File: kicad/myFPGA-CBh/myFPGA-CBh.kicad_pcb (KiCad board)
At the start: 2 copper layers, 100 x 80 mm, 62 parts, among them J1 Conn_01x04, J10 Conn_01x04, J11 Conn_01x04, J12 Conn_01x04, J13 Conn_01x04, J14 Conn_01x04, J15 Conn_01x04, J2 Conn_01x04, J3 Conn_01x04, J4 Conn_01x04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

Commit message: start new feature CE
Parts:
- added D16: LED (green), LED_SMD:LED_0805_2012Metric, F.Cu at (177.0, 114.0)
- added J16: Conn_01x02, Connector_PinHeader_2.54mm:PinHeader_1x02_P2.54mm_Horizontal, F.Cu at (181.5, 125.0)
- added R16: 330R, Resistor_SMD:R_0603_1608Metric, F.Cu at (173.0, 115.0)
- added U10: BL1551B, Package_TO_SOT_SMD:SOT-363_SC-70-6, F.Cu at (177.0, 116.6)
- U7, U8, U9: value NC7SB3157P6X -> BL1551B
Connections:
- J7 pad 1: prio_0 -> bus_4
- J7 pad 2: prio_1 -> bus_5
- J8 pad 1: prio_1 -> bus_5
- J8 pad 2: prio_0 -> bus_4
- U2 pad 7: unconnected-(U2-QH-Pad7) -> xp_ce
- U3 pad 1: prio_0 -> unconnected-(U3-I3-Pad1)
- U3 pad 2: prio_1 -> unconnected-(U3-I2-Pad2)
- U4 pad 1: prio_0 -> bus_4
- U4 pad 2: prio_1 -> bus_5
- U5 pad 1: prio_0 -> bus_4
- U5 pad 2: prio_1 -> bus_5
- U6 pad 1: prio_0 -> bus_4
- U6 pad 2: prio_1 -> bus_5
- U7 pad 4: prio_0 -> bus_4
- U8 pad 4: prio_1 -> bus_5
- U9 pad 4: prio_0 -> bus_4
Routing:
- net (no net): track 0.00 -> 415.0 mm, vias 0 -> 13
- net prio_0: track 214.8 -> 0.00 mm, vias 7 -> 0
- net prio_1: track 200.3 -> 0.00 mm, vias 6 -> 0
- net xp_ce: track 0.00 -> 73.4 mm, vias 0 -> 2
- net GND: track 514.0 -> 522.2 mm, vias 16 -> 17
- net ce: track 0.00 -> 8.19 mm
- net +3.3VP: track 145.2 -> 148.7 mm, vias 13 -> 14
- net Net-(D16-A): track 0.00 -> 3.13 mm
- net aresetn: track 69.3 -> 72.2 mm

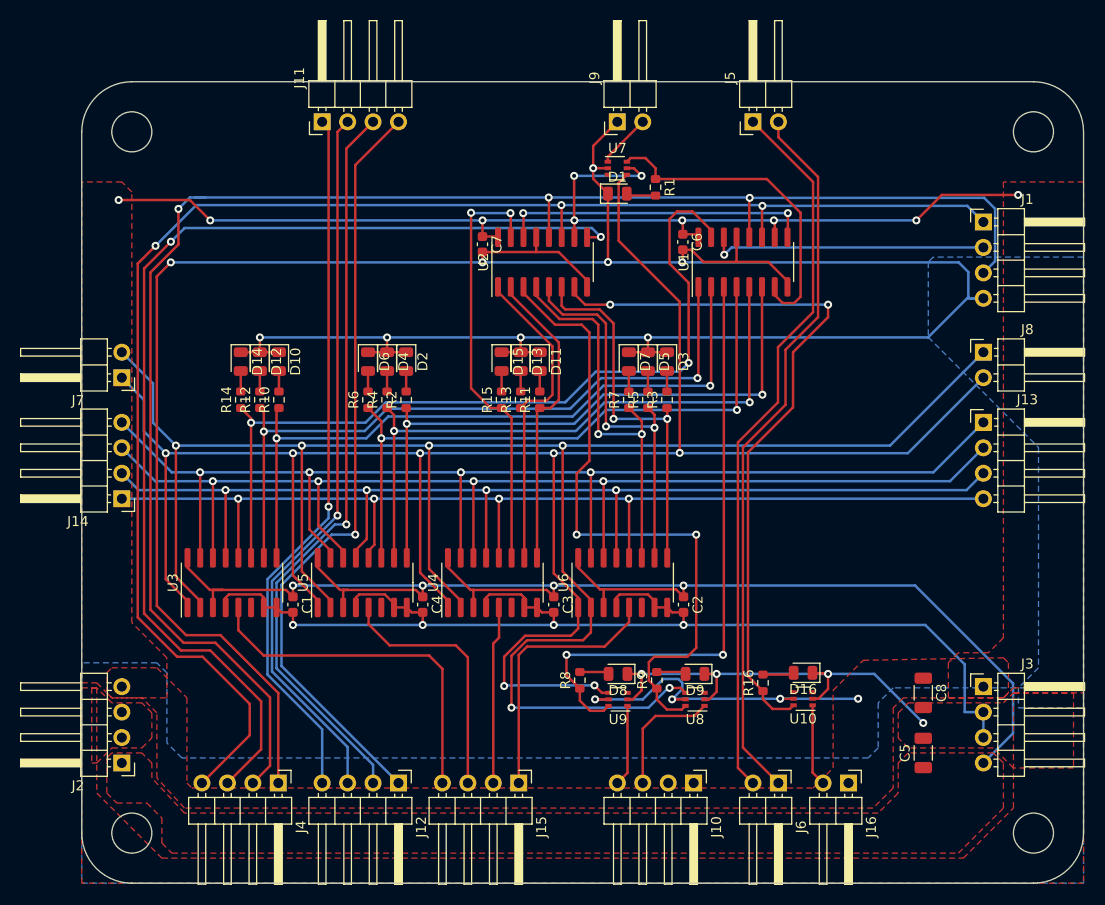
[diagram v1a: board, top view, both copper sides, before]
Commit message: found more bugs
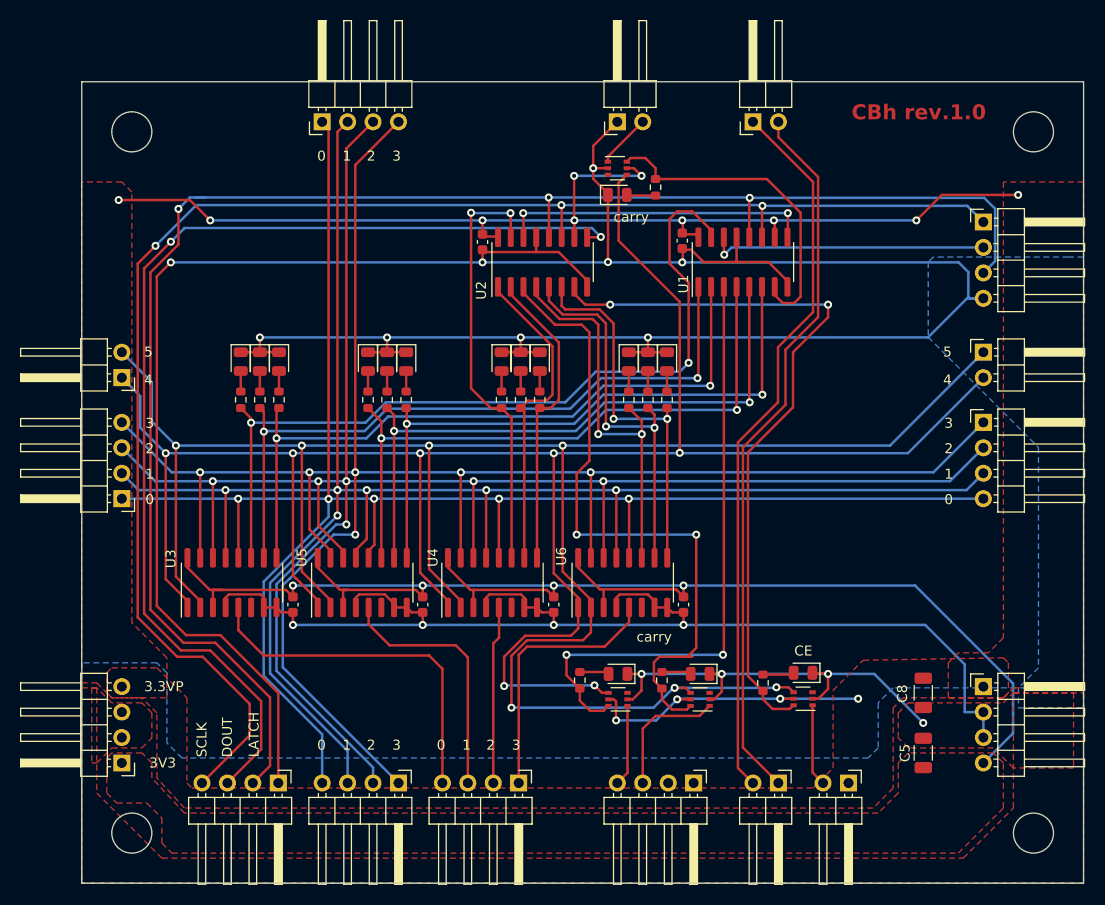
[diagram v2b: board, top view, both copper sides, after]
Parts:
- moved D9 0.51 mm to (166.7, 114.1)
- moved R9 0.51 mm to (162.9, 114.7)
- moved U8 0.51 mm to (166.7, 116.7)
- moved C7 0.23 mm to (145.0, 71.0)
- moved C6 0.14 mm to (164.9, 70.9)
- moved D1 0.13 mm to (158.5, 66.3)
- renumbered R6 to Re, J10 to locked, J5 to locked, J15 to locked, J4 to locked
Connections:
- J11 pad 1: Net-(J11-Pin_1) -> bus_0
- J11 pad 2: Net-(J11-Pin_2) -> bus_1
- J11 pad 3: Net-(J11-Pin_3) -> bus_2
- J11 pad 4: Net-(J11-Pin_4) -> bus_3
- J12 pad 1: Net-(J11-Pin_4) -> bus_3
- J12 pad 2: Net-(J11-Pin_3) -> bus_2
- J12 pad 3: Net-(J11-Pin_2) -> bus_1
- J12 pad 4: Net-(J11-Pin_1) -> bus_0
- U3 pad 1: unconnected-(U3-I3-Pad1) -> bus_4
- U3 pad 2: unconnected-(U3-I2-Pad2) -> bus_5
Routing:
- net (no net): track 415.0 -> 0.00 mm, vias 13 -> 0
- net bus_4: track 0.00 -> 214.8 mm, vias 0 -> 7
- net bus_5: track 0.00 -> 212.9 mm, vias 0 -> 7
- net Net-(J11-Pin_4): track 77.1 -> 0.00 mm, vias 1 -> 0
- net bus_3: track 125.2 -> 202.0 mm, vias 4 -> 6
- net Net-(J11-Pin_3): track 74.7 -> 0.00 mm, vias 1 -> 0
- net bus_2: track 120.4 -> 195.0 mm, vias 4 -> 6
- net bus_1: track 114.9 -> 187.3 mm, vias 4 -> 6
- net Net-(J11-Pin_2): track 72.3 -> 0.00 mm, vias 1 -> 0
- net bus_0: track 109.9 -> 181.3 mm, vias 4 -> 5
- net Net-(J11-Pin_1): track 71.1 -> 0.00 mm, vias 1 -> 0
- net +3.3VP: track 148.7 -> 144.8 mm
- net cout_s: track 12.5 -> 13.0 mm
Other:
- outline, holes or cut-outs redrawn
- board text added: "0"
- board text added: "1"
- board text added: "2"
- board text added: "3"
- board text added: "3.3VP"
- board text added: "3V3"
- board text added: "4"
- board text added: "5"
- board text added: "CBh rev.1.0"
- board text added: "CE"
- board text added: "DOUT"
- board text added: "LATCH"
- board text added: "SCLK"
- board text added: "carry"
